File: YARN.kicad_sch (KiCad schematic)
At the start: 34 parts, among them J1 Cart System Out, J2 Cart Sub In, J3 Cart Main In, U1 EXP Addressing Decoder ROM

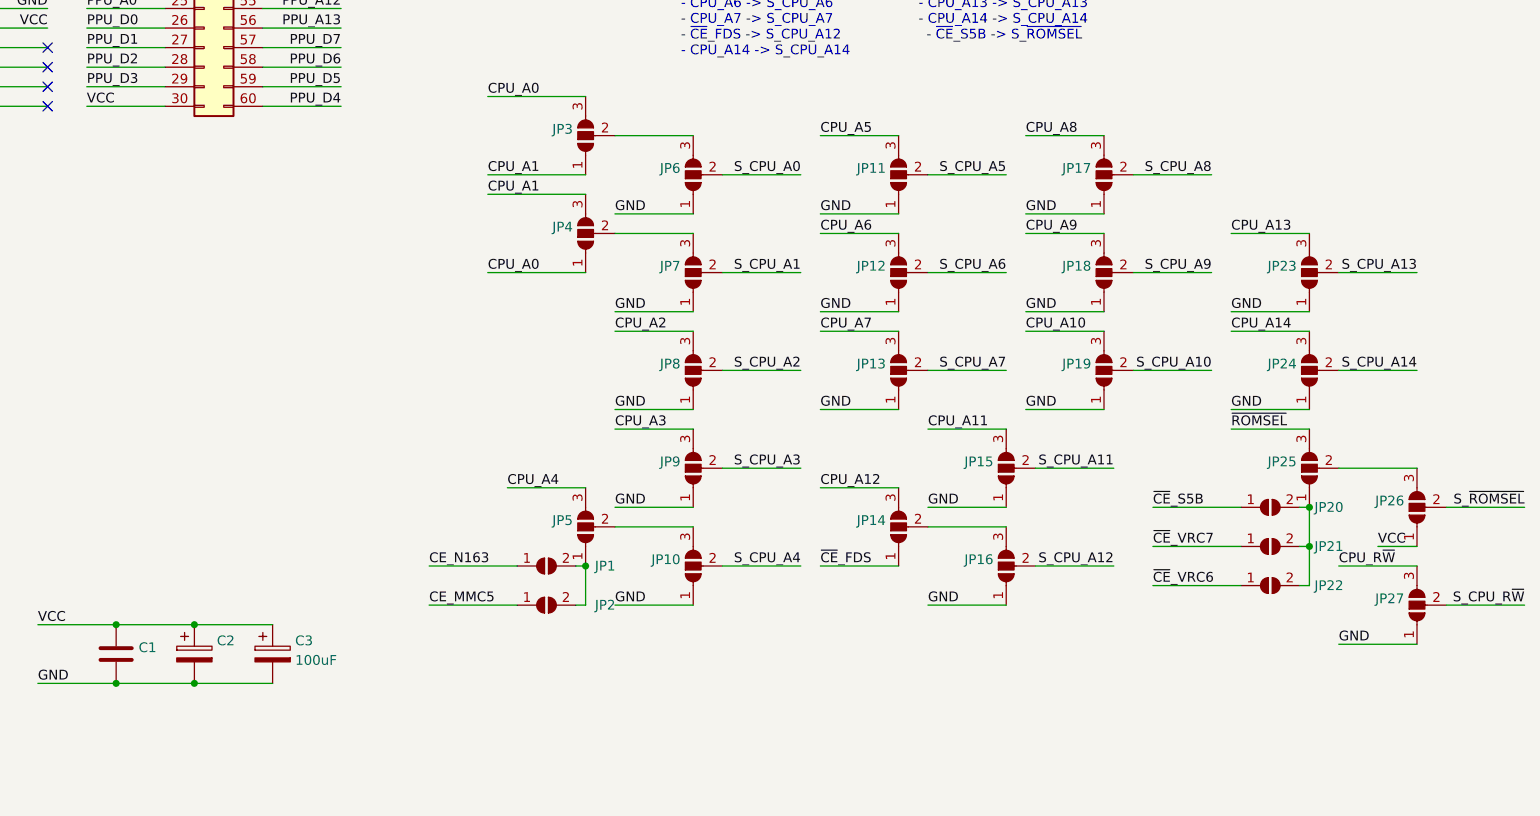
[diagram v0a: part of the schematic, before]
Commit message: Fix copper fills
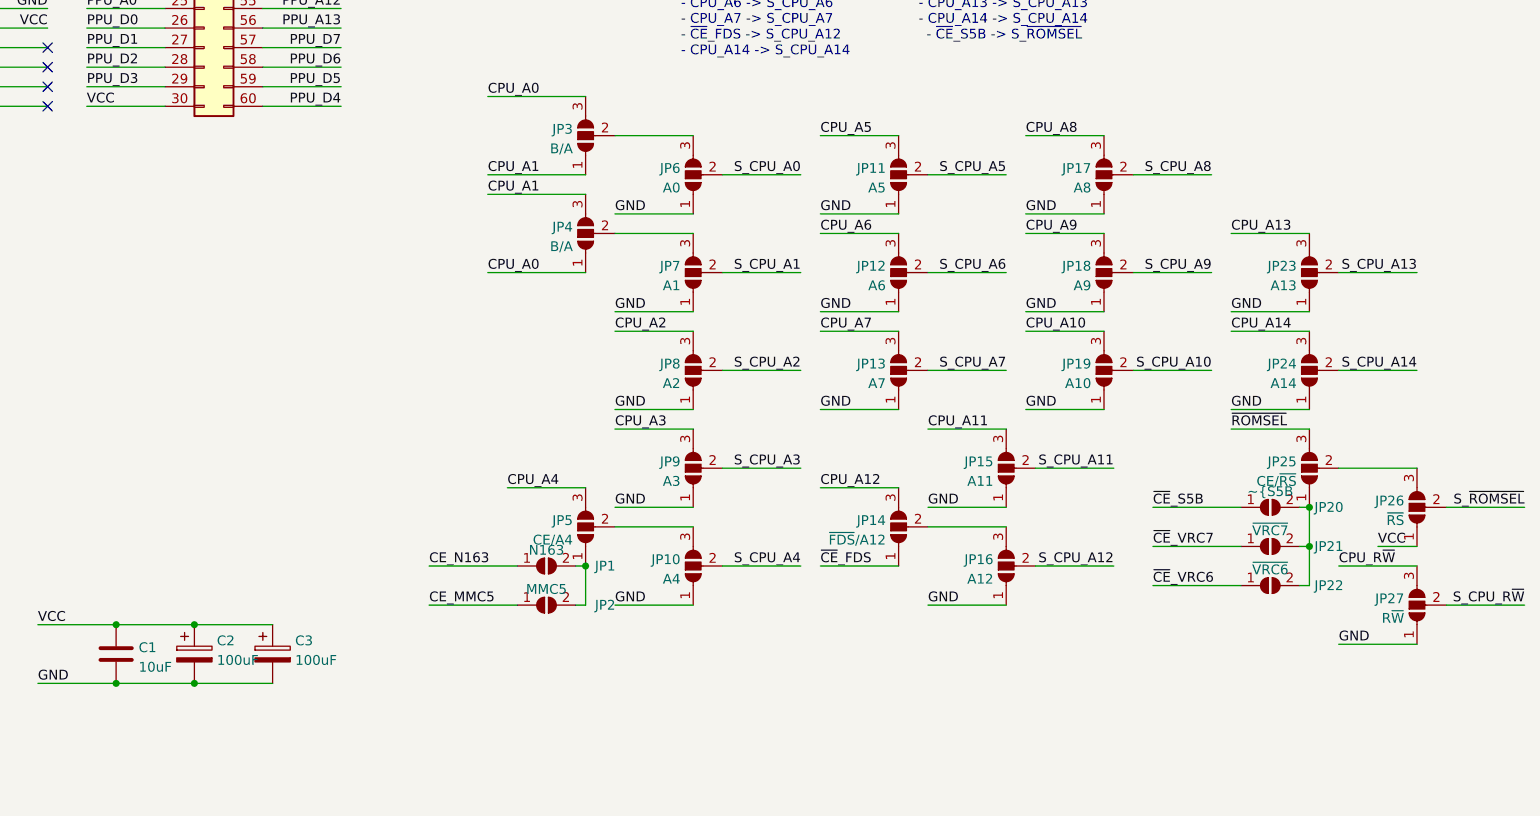
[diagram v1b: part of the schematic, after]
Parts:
- C1: value (none) -> 10uF; footprint (none) -> YARN:C_Disc-0805_D3.0mm_W1.6mm_P2.50mm
- C2: value (none) -> 100uF; footprint (none) -> Capacitor_THT:CP_Radial_D5.0mm_P2.50mm
- JP1: value (none) -> N163; footprint (none) -> Jumper:SolderJumper-2_P1.3mm_Open_Pad1.0x1.5mm
- JP10: value (none) -> A4; footprint (none) -> Jumper:SolderJumper-3_P1.3mm_Open_Pad1.0x1.5mm
- JP11: value (none) -> A5; footprint (none) -> Jumper:SolderJumper-3_P1.3mm_Open_Pad1.0x1.5mm
- JP12: value (none) -> A6; footprint (none) -> Jumper:SolderJumper-3_P1.3mm_Open_Pad1.0x1.5mm
- JP13: value (none) -> A7; footprint (none) -> Jumper:SolderJumper-3_P1.3mm_Open_Pad1.0x1.5mm
- JP14: value (none) -> ~{FDS}/A12; footprint (none) -> Jumper:SolderJumper-3_P1.3mm_Open_Pad1.0x1.5mm
- JP15: value (none) -> A11; footprint (none) -> Jumper:SolderJumper-3_P1.3mm_Open_Pad1.0x1.5mm
- JP16: value (none) -> A12; footprint (none) -> Jumper:SolderJumper-3_P1.3mm_Open_Pad1.0x1.5mm
- JP17: value (none) -> A8; footprint (none) -> Jumper:SolderJumper-3_P1.3mm_Open_Pad1.0x1.5mm
- JP18: value (none) -> A9; footprint (none) -> Jumper:SolderJumper-3_P1.3mm_Open_Pad1.0x1.5mm
- JP19: value (none) -> A10; footprint (none) -> Jumper:SolderJumper-3_P1.3mm_Open_Pad1.0x1.5mm
- JP2: value (none) -> MMC5; footprint (none) -> Jumper:SolderJumper-2_P1.3mm_Open_Pad1.0x1.5mm
- JP20: value (none) -> ~{S5B; footprint (none) -> Jumper:SolderJumper-2_P1.3mm_Open_Pad1.0x1.5mm
- JP21: value (none) -> ~{VRC7}; footprint (none) -> Jumper:SolderJumper-2_P1.3mm_Open_Pad1.0x1.5mm
- JP22: value (none) -> ~{VRC6}; footprint (none) -> Jumper:SolderJumper-2_P1.3mm_Open_Pad1.0x1.5mm
- JP23: value (none) -> A13; footprint (none) -> Jumper:SolderJumper-3_P1.3mm_Open_Pad1.0x1.5mm
- JP24: value (none) -> A14; footprint (none) -> Jumper:SolderJumper-3_P1.3mm_Open_Pad1.0x1.5mm
- JP25: value (none) -> CE/~{RS}; footprint (none) -> Jumper:SolderJumper-3_P1.3mm_Open_Pad1.0x1.5mm
- JP26: value (none) -> ~{RS}; footprint (none) -> Jumper:SolderJumper-3_P1.3mm_Open_Pad1.0x1.5mm
- JP27: value (none) -> R~{W}; footprint (none) -> Jumper:SolderJumper-3_P1.3mm_Open_Pad1.0x1.5mm
- JP3, JP4: value (none) -> B/A; footprint (none) -> Jumper:SolderJumper-3_P1.3mm_Open_Pad1.0x1.5mm
- JP5: value (none) -> CE/A4; footprint (none) -> Jumper:SolderJumper-3_P1.3mm_Open_Pad1.0x1.5mm
- JP6: value (none) -> A0; footprint (none) -> Jumper:SolderJumper-3_P1.3mm_Open_Pad1.0x1.5mm
- JP7: value (none) -> A1; footprint (none) -> Jumper:SolderJumper-3_P1.3mm_Open_Pad1.0x1.5mm
- JP8: value (none) -> A2; footprint (none) -> Jumper:SolderJumper-3_P1.3mm_Open_Pad1.0x1.5mm
- JP9: value (none) -> A3; footprint (none) -> Jumper:SolderJumper-3_P1.3mm_Open_Pad1.0x1.5mm

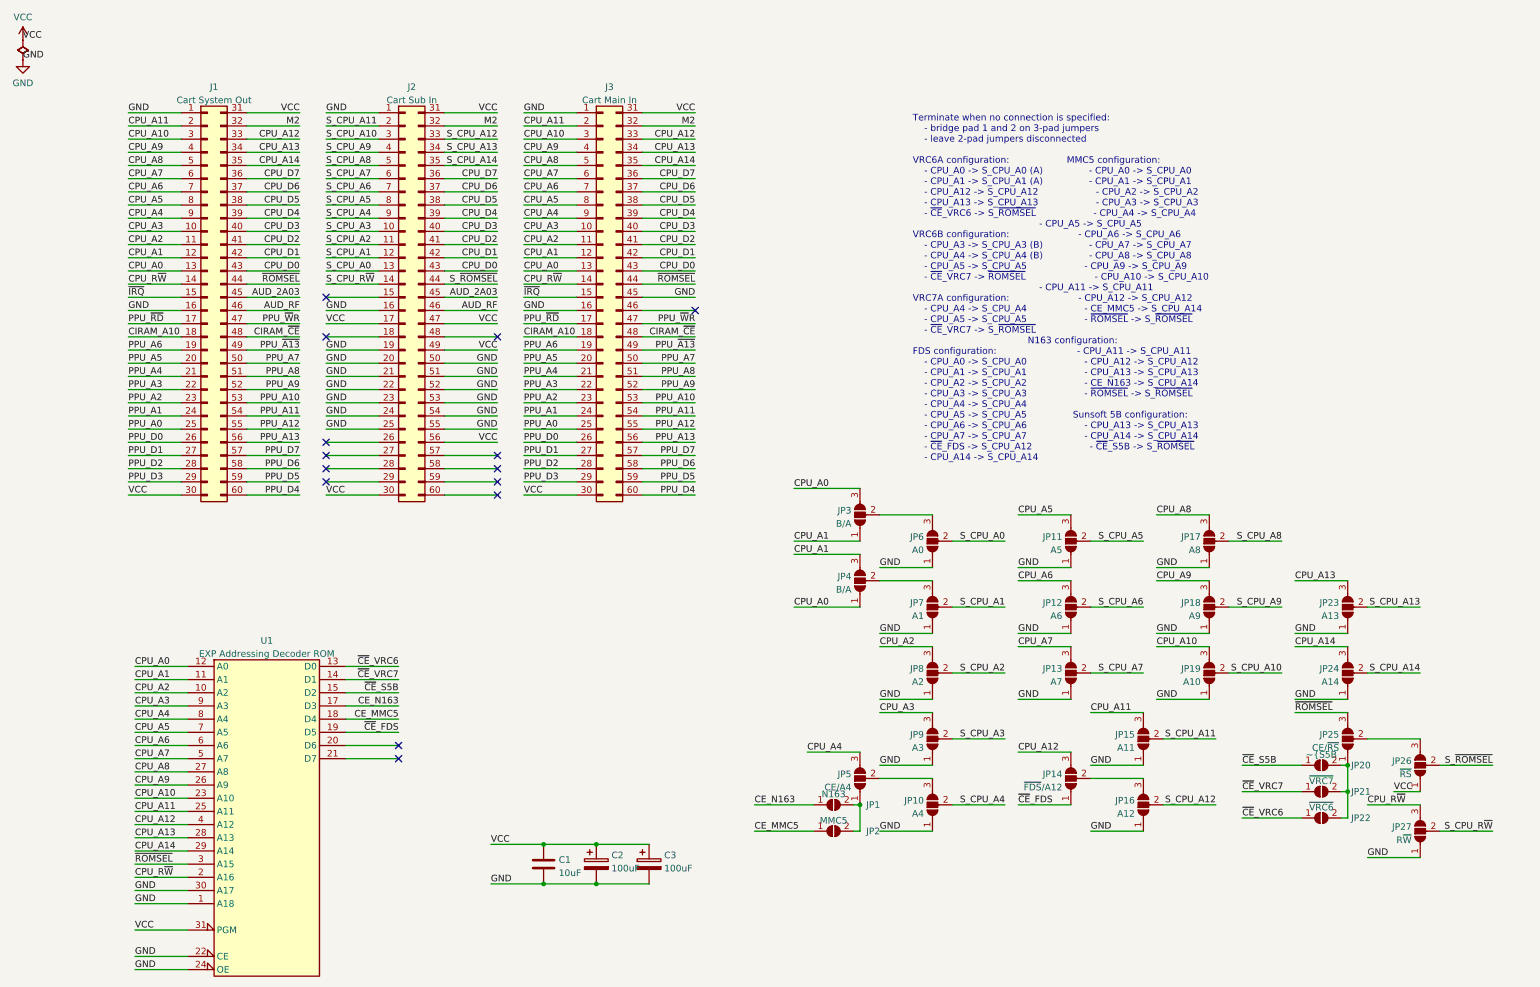
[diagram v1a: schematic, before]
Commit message: Use bus buffers instead of decoding logic
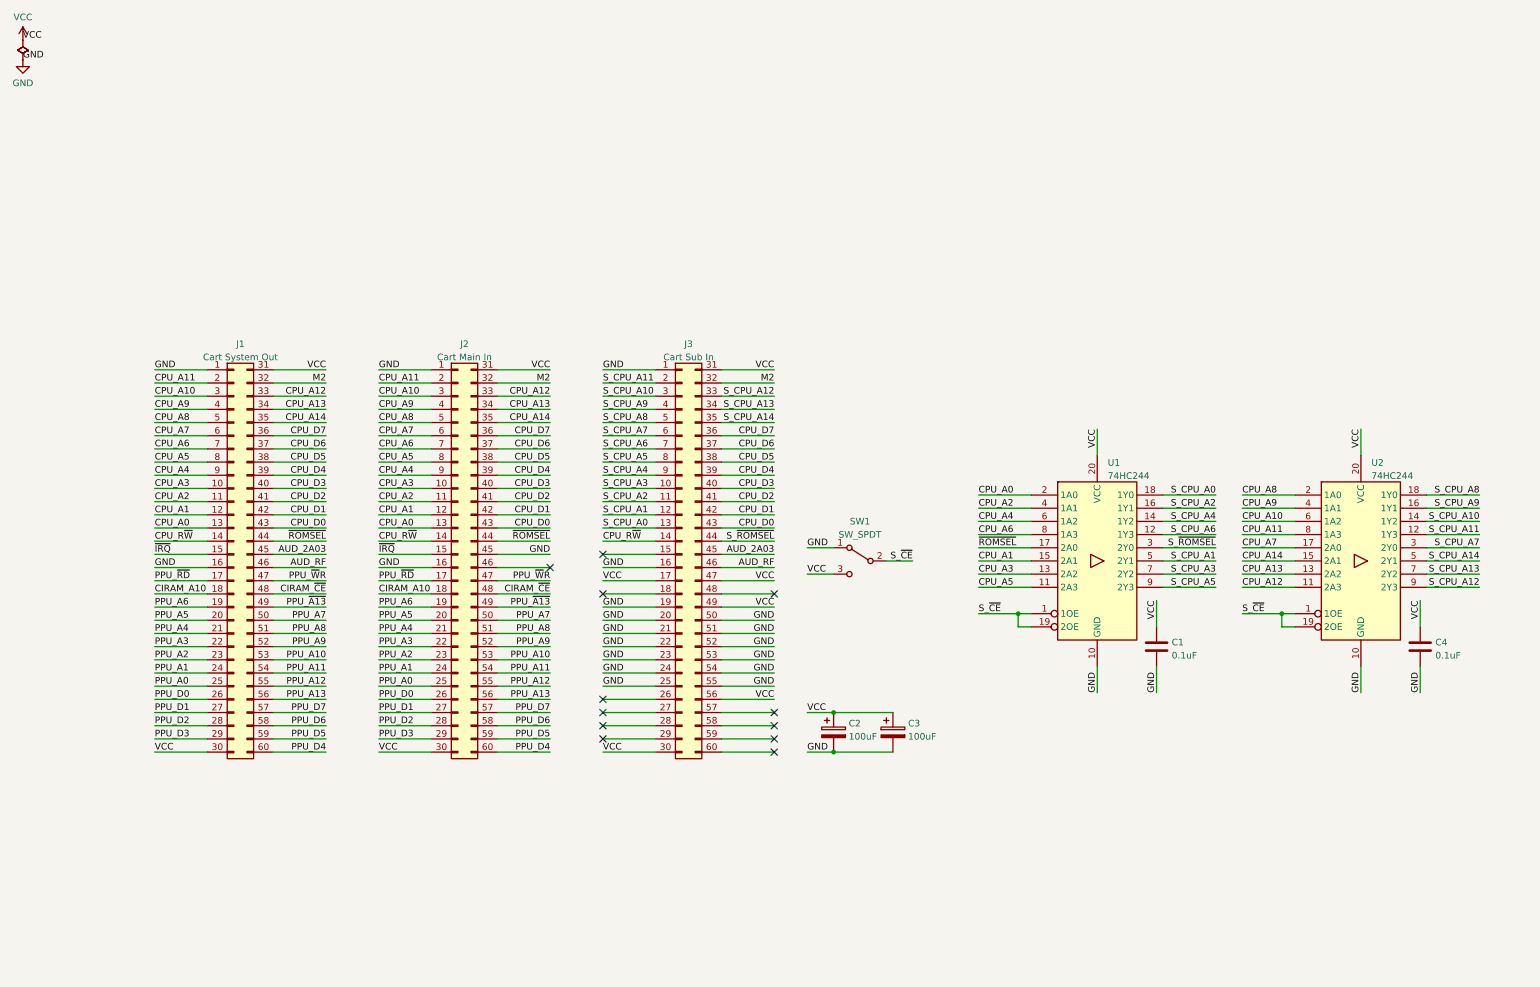
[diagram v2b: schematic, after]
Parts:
- removed JP1: N163, Jumper:SolderJumper-2_P1.3mm_Open_Pad1.0x1.5mm, symbol Jumper:SolderJumper_2_Open
- removed JP10: A4, Jumper:SolderJumper-3_P1.3mm_Open_Pad1.0x1.5mm, symbol Jumper:SolderJumper_3_Open
- removed JP11: A5, Jumper:SolderJumper-3_P1.3mm_Open_Pad1.0x1.5mm, symbol Jumper:SolderJumper_3_Open
- removed JP12: A6, Jumper:SolderJumper-3_P1.3mm_Open_Pad1.0x1.5mm, symbol Jumper:SolderJumper_3_Open
- removed JP13: A7, Jumper:SolderJumper-3_P1.3mm_Open_Pad1.0x1.5mm, symbol Jumper:SolderJumper_3_Open
- removed JP14: ~{FDS}/A12, Jumper:SolderJumper-3_P1.3mm_Open_Pad1.0x1.5mm, symbol Jumper:SolderJumper_3_Open
- removed JP15: A11, Jumper:SolderJumper-3_P1.3mm_Open_Pad1.0x1.5mm, symbol Jumper:SolderJumper_3_Open
- removed JP16: A12, Jumper:SolderJumper-3_P1.3mm_Open_Pad1.0x1.5mm, symbol Jumper:SolderJumper_3_Open
- removed JP17: A8, Jumper:SolderJumper-3_P1.3mm_Open_Pad1.0x1.5mm, symbol Jumper:SolderJumper_3_Open
- removed JP18: A9, Jumper:SolderJumper-3_P1.3mm_Open_Pad1.0x1.5mm, symbol Jumper:SolderJumper_3_Open
- removed JP19: A10, Jumper:SolderJumper-3_P1.3mm_Open_Pad1.0x1.5mm, symbol Jumper:SolderJumper_3_Open
- removed JP2: MMC5, Jumper:SolderJumper-2_P1.3mm_Open_Pad1.0x1.5mm, symbol Jumper:SolderJumper_2_Open
- removed JP20: ~{S5B, Jumper:SolderJumper-2_P1.3mm_Open_Pad1.0x1.5mm, symbol Jumper:SolderJumper_2_Open
- removed JP21: ~{VRC7}, Jumper:SolderJumper-2_P1.3mm_Open_Pad1.0x1.5mm, symbol Jumper:SolderJumper_2_Open
- removed JP22: ~{VRC6}, Jumper:SolderJumper-2_P1.3mm_Open_Pad1.0x1.5mm, symbol Jumper:SolderJumper_2_Open
- removed JP23: A13, Jumper:SolderJumper-3_P1.3mm_Open_Pad1.0x1.5mm, symbol Jumper:SolderJumper_3_Open
- removed JP24: A14, Jumper:SolderJumper-3_P1.3mm_Open_Pad1.0x1.5mm, symbol Jumper:SolderJumper_3_Open
- removed JP25: CE/~{RS}, Jumper:SolderJumper-3_P1.3mm_Open_Pad1.0x1.5mm, symbol Jumper:SolderJumper_3_Open
- removed JP26: ~{RS}, Jumper:SolderJumper-3_P1.3mm_Open_Pad1.0x1.5mm, symbol Jumper:SolderJumper_3_Open
- removed JP27: R~{W}, Jumper:SolderJumper-3_P1.3mm_Open_Pad1.0x1.5mm, symbol Jumper:SolderJumper_3_Open
- removed JP3, JP4: B/A, Jumper:SolderJumper-3_P1.3mm_Open_Pad1.0x1.5mm, symbol Jumper:SolderJumper_3_Open
- removed JP5: CE/A4, Jumper:SolderJumper-3_P1.3mm_Open_Pad1.0x1.5mm, symbol Jumper:SolderJumper_3_Open
- removed JP6: A0, Jumper:SolderJumper-3_P1.3mm_Open_Pad1.0x1.5mm, symbol Jumper:SolderJumper_3_Open
- removed JP7: A1, Jumper:SolderJumper-3_P1.3mm_Open_Pad1.0x1.5mm, symbol Jumper:SolderJumper_3_Open
- removed JP8: A2, Jumper:SolderJumper-3_P1.3mm_Open_Pad1.0x1.5mm, symbol Jumper:SolderJumper_3_Open
- removed JP9: A3, Jumper:SolderJumper-3_P1.3mm_Open_Pad1.0x1.5mm, symbol Jumper:SolderJumper_3_Open
- removed U1: EXP Addressing Decoder ROM, Package_DIP:DIP-32_W15.24mm_Socket_LongPads, symbol Memory_Flash:SST39SF040
- added C4: 0.1uF, YARN:C_Disc-0805_D3.0mm_W1.6mm_P2.50mm, symbol Device:C
- added SW1: SW_SPDT, YARN:JS102011SCQN, symbol Switch:SW_SPDT
- added U1, U2: 74HC244, Package_SO:SOIC-20W_7.5x12.8mm_P1.27mm, symbol 74xx:74HC244
- C1: value 10uF -> 0.1uF
- renumbered J3 to J2, J2 to J3
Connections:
- net S_CPU_R~{W} is gone; now on net CPU_R~{W}: J3.14 (Pin_14)
- net CPU_A0: now also U1.2 (1A0)
- net CPU_A1: now also U1.15 (2A1)
- net CPU_A10: now also U2.6 (1A2)
- net CPU_A11: now also U2.8 (1A3)
- net CPU_A12: now also U2.11 (2A3)
- net CPU_A13: now also U2.13 (2A2)
- net CPU_A14: now also U2.15 (2A1)
- net CPU_A2: now also U1.4 (1A1)
- net CPU_A3: now also U1.13 (2A2)
- net CPU_A4: now also U1.6 (1A2)
- net CPU_A5: now also U1.11 (2A3)
- net CPU_A6: now also U1.8 (1A3)
- net CPU_A7: now also U2.17 (2A0)
- net CPU_A8: now also U2.2 (1A0)
- net CPU_A9: now also U2.4 (1A1)
- net GND: now also C4.2, SW1.1 (A), U1.10 (GND), U2.10 (GND)
- net S_CPU_A0: now also U1.18 (1Y0)
- net S_CPU_A1: now also U1.5 (2Y1)
- net S_CPU_A10: now also U2.14 (1Y2)
- net S_CPU_A11: now also U2.12 (1Y3)
- net S_CPU_A12: now also U2.9 (2Y3)
- net S_CPU_A13: now also U2.7 (2Y2)
- net S_CPU_A14: now also U2.5 (2Y1)
- net S_CPU_A2: now also U1.16 (1Y1)
- net S_CPU_A3: now also U1.7 (2Y2)
- net S_CPU_A4: now also U1.14 (1Y2)
- net S_CPU_A5: now also U1.9 (2Y3)
- net S_CPU_A6: now also U1.12 (1Y3)
- net S_CPU_A7: now also U2.3 (2Y0)
- net S_CPU_A8: now also U2.18 (1Y0)
- net S_CPU_A9: now also U2.16 (1Y1)
- net S_~{ROMSEL}: now also U1.3 (2Y0)
- net VCC: now also C4.1, SW1.3 (C), U1.20 (VCC), U2.20 (VCC)
- net ~{ROMSEL}: now also U1.17 (2A0)
- new net S_~{CE}: SW1.2 (B), U1.1 (1OE), U1.19 (2OE), U2.1 (1OE), U2.19 (2OE)
- no-connect marks 14 -> 12
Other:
- note removed: "Terminate when no connection is specified: - bridge pad 1 and 2 on 3-pad jumpers - leave 2-pad jumpers disconnected VRC6A configuration: MMC5 configuration: - CPU_A0 -> S_CPU_A0 (A) - CPU_A0 -> S_CPU_A0 - CPU_A1 -> S_CPU_A1 (A) - CPU_A1 -> S_CPU_A1 - CPU_A12 -> S_CPU_A12 - CPU_A2 -> S_CPU_A2 - CPU_A13 -> S_CPU_A13 - CPU_A3 -> S_CPU_A3 - ~{CE}_VRC6 -> S_~{ROMSEL} - CPU_A4 -> S_CPU_A4 - CPU_A5 -> S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"
- company: (none) -> Persune
- title: YARN -> Y-Adaptive Receiving Nexus
- moved on the sheet: C1, C2, C3, J1, J2, J3
